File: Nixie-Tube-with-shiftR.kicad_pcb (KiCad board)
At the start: 2 copper layers, 37 x 44 mm, 55 parts, among them J1 Conn_01x06_Male, J2 Conn_01x01_Female, J3 Conn_01x06_Female, J4 Conn_01x01_Male, Q1 MMBTA42LT1, Q10 MMBTA42LT1, Q11 AO3400, Q12 AO3400, Q13 AO3400, Q14 MMBTA42LT1, Q15 MMBTA42LT1, Q2 MMBTA42LT1, Q3 MMBTA42LT1, Q4 MMBTA42LT1, Q5 MMBTA42LT1, Q6 MMBTA42LT1, Q7 MMBTA42LT1, Q8 MMBTA42LT1, Q9 MMBTA42LT1, U1 74HC595D, U2 nixie-tube, U3 74HC595D, U4 ams1117-5.0

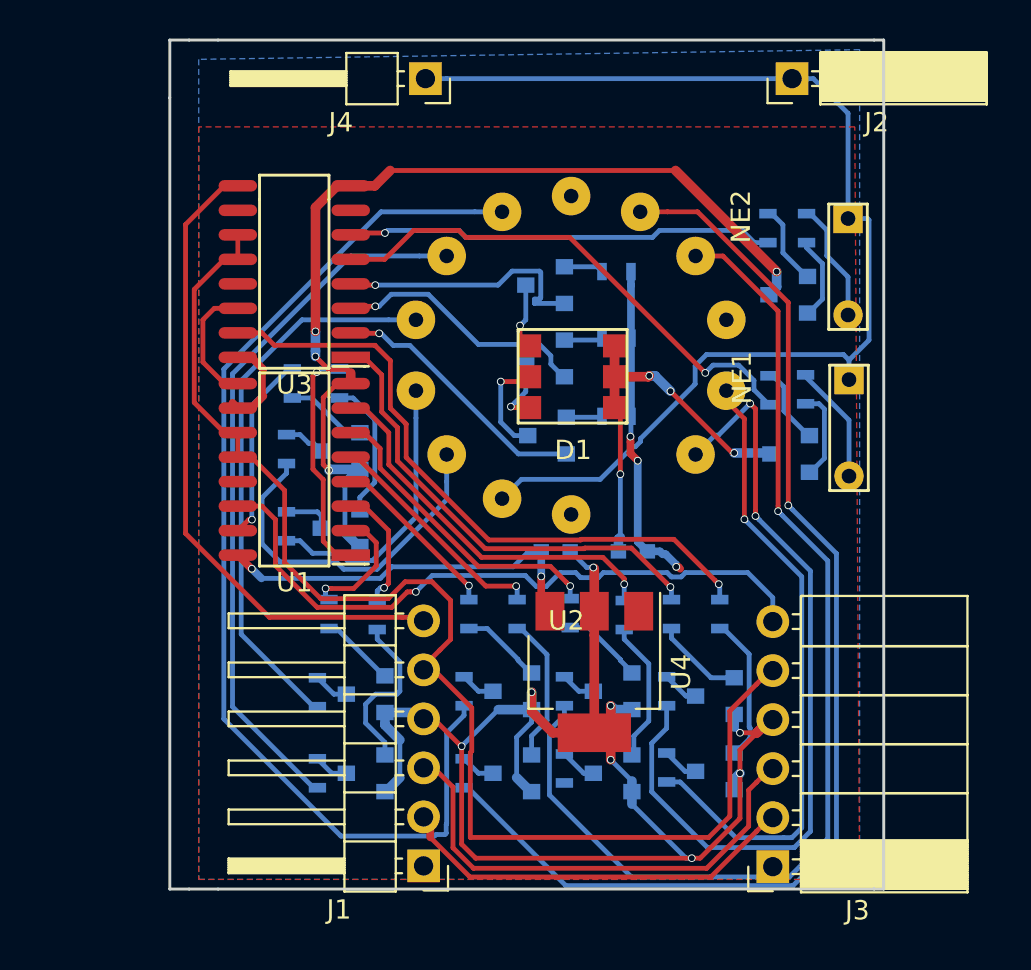
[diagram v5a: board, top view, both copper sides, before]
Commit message: placement of resistor
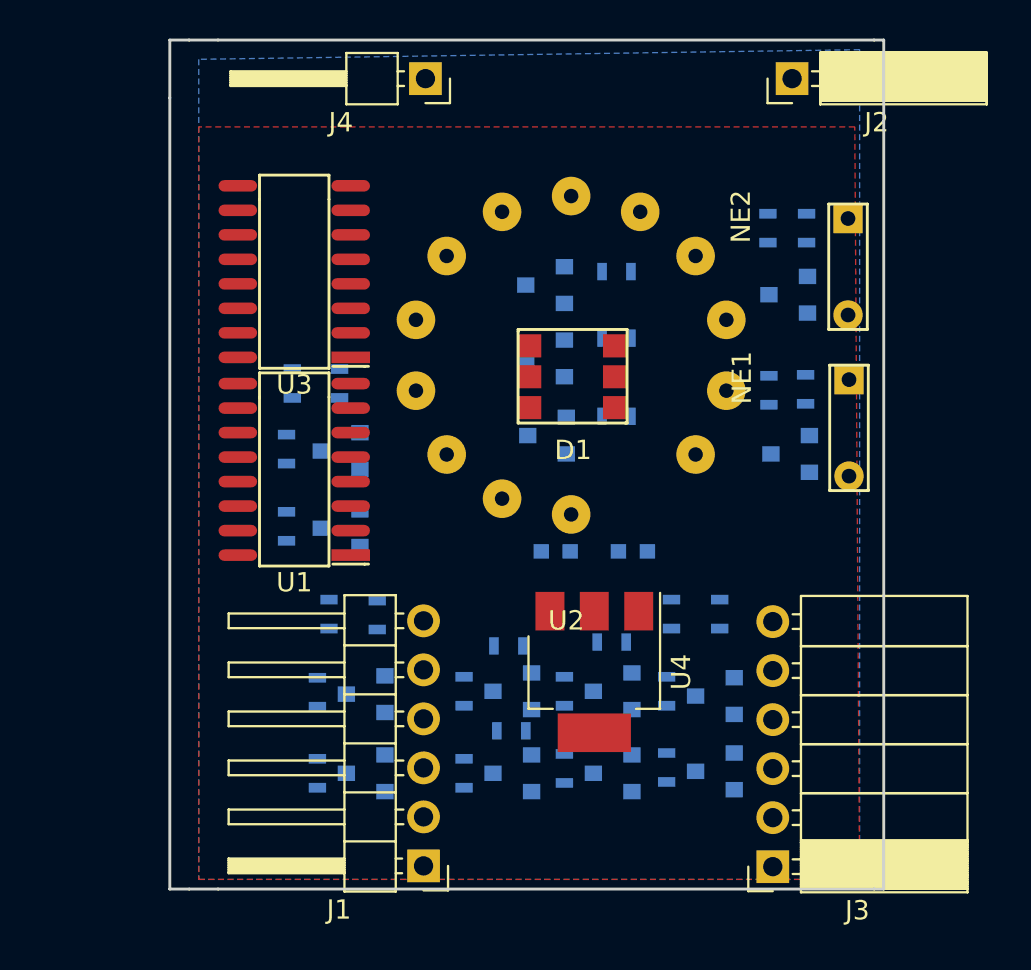
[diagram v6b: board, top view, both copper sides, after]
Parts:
- moved R18 6.25 mm to (174.3, 80.0), turned to 0 degrees
- moved R15 6.06 mm to (169.2, 79.8), turned to 0 degrees
- moved R23 2.63 mm to (169.1, 75.4), turned to 0 degrees
- moved R17 2.62 mm to (174.4, 75.2), turned to 0 degrees
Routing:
- net GND: track 147.8 -> 0.00 mm, vias 16 -> 0
- net /SCK: track 67.5 -> 0.00 mm
- net Net-(R6-Pad1): track 61.0 -> 0.00 mm, vias 1 -> 0
- net Net-(J2-Pad1): track 59.7 -> 0.00 mm
- net Net-(R5-Pad1): track 57.0 -> 0.00 mm
- net Net-(R7-Pad1): track 55.8 -> 0.00 mm, vias 1 -> 0
- net Net-(R10-Pad1): track 41.9 -> 0.00 mm, vias 2 -> 0
- net +9V: track 38.2 -> 0.00 mm, vias 3 -> 0
- net Net-(R4-Pad1): track 37.0 -> 0.00 mm
- net /MOSI: track 34.6 -> 0.00 mm, vias 1 -> 0
- net /MOSI-OUT: track 33.7 -> 0.00 mm
- net /s1: track 33.6 -> 0.00 mm, vias 1 -> 0
- net Net-(R9-Pad1): track 32.7 -> 0.00 mm, vias 1 -> 0
- net Net-(R3-Pad1): track 29.0 -> 0.00 mm
- net +5V: track 26.7 -> 0.00 mm, vias 2 -> 0
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
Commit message: change the sequence of s0-s9
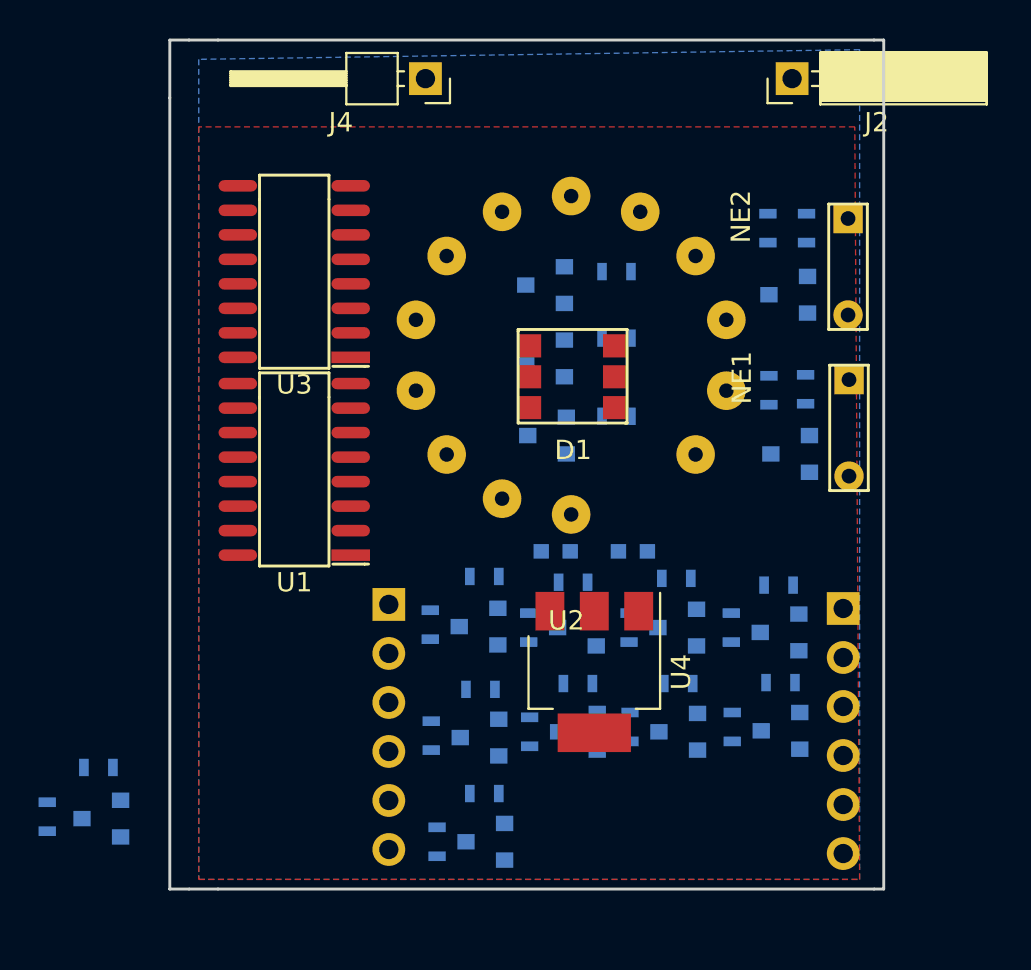
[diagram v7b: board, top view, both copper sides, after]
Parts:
- J1, J3: moved to B.Cu
- moved Q1 22.7 mm to (147.9, 84.3)
- moved R1 22.7 mm to (145.2, 84.2)
- moved R14 22.3 mm to (147.8, 81.7), turned to 180 degrees
- moved J3 13.9 mm to (186.4, 73.5)
- moved J1 13.7 mm to (162.8, 73.2)
- moved R16 12.5 mm to (167.8, 71.8), turned to 0 degrees
- moved R21 10.8 mm to (167.8, 83.0), turned to 0 degrees
- moved R2 9.03 mm to (165.0, 74.3)
- moved Q3 8.78 mm to (167.5, 74.4)
- moved R19 8.77 mm to (167.6, 77.7), turned to 0 degrees
- moved Q8 7.14 mm to (167.8, 85.5)
- moved R4 7.14 mm to (165.3, 85.5)
- moved Q6 6.31 mm to (167.6, 80.2)
- moved R3 6.31 mm to (165.1, 80.0)
- moved R22 5.75 mm to (183.1, 72.2), turned to 0 degrees
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
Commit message: move shift reg to bottom
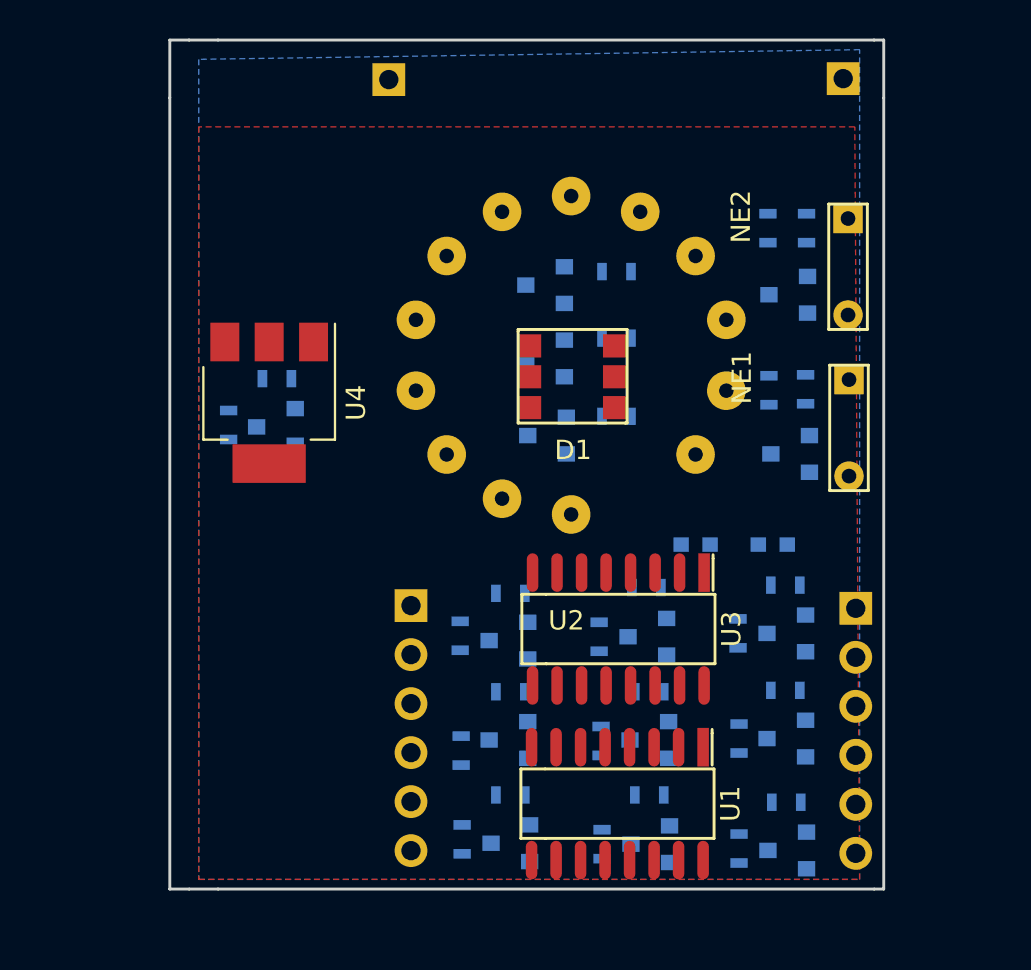
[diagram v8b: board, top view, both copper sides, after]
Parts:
- J2, J4: moved to B.Cu
- moved U3 25.0 mm to (174.7, 74.5), turned to 270 degrees
- moved U1 24.1 mm to (174.7, 83.6), turned to 270 degrees
- moved R1 22.4 mm to (154.6, 64.0)
- moved Q1 22.2 mm to (157.0, 64.0)
- moved R14 22.2 mm to (157.1, 61.5)
- moved U4 21.9 mm to (156.7, 62.8)
- moved R2 19.8 mm to (181.0, 85.9)
- moved Q3 19.8 mm to (183.5, 86.0)
- moved R16 19.5 mm to (183.4, 83.5)
- moved Q8 19.0 mm to (183.4, 74.8)
- moved R21 19.0 mm to (183.4, 72.2)
- moved R4 19.0 mm to (180.9, 74.8)
- moved R3 16.0 mm to (181.0, 80.2)
- moved Q6 15.9 mm to (183.4, 80.2)
- moved R19 15.8 mm to (183.4, 77.7)
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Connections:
- U1 pad 1: /s8 -> /s1
- U1 pad 15: /s9 -> /s0
- U1 pad 2: /s7 -> /s2
- U1 pad 3: /s6 -> /s3
- U1 pad 4: /s5 -> /s4
- U1 pad 5: /s4 -> /s5
- U1 pad 6: /s3 -> /s6
- U1 pad 7: /s2 -> /s7
- U3 pad 1: /s0 -> /s9
- U3 pad 15: /s1 -> /s8
